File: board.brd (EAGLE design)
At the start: 100 x 80 mm, 11 parts, among them CON1 Power, SW1 PROG, SW2 RESET

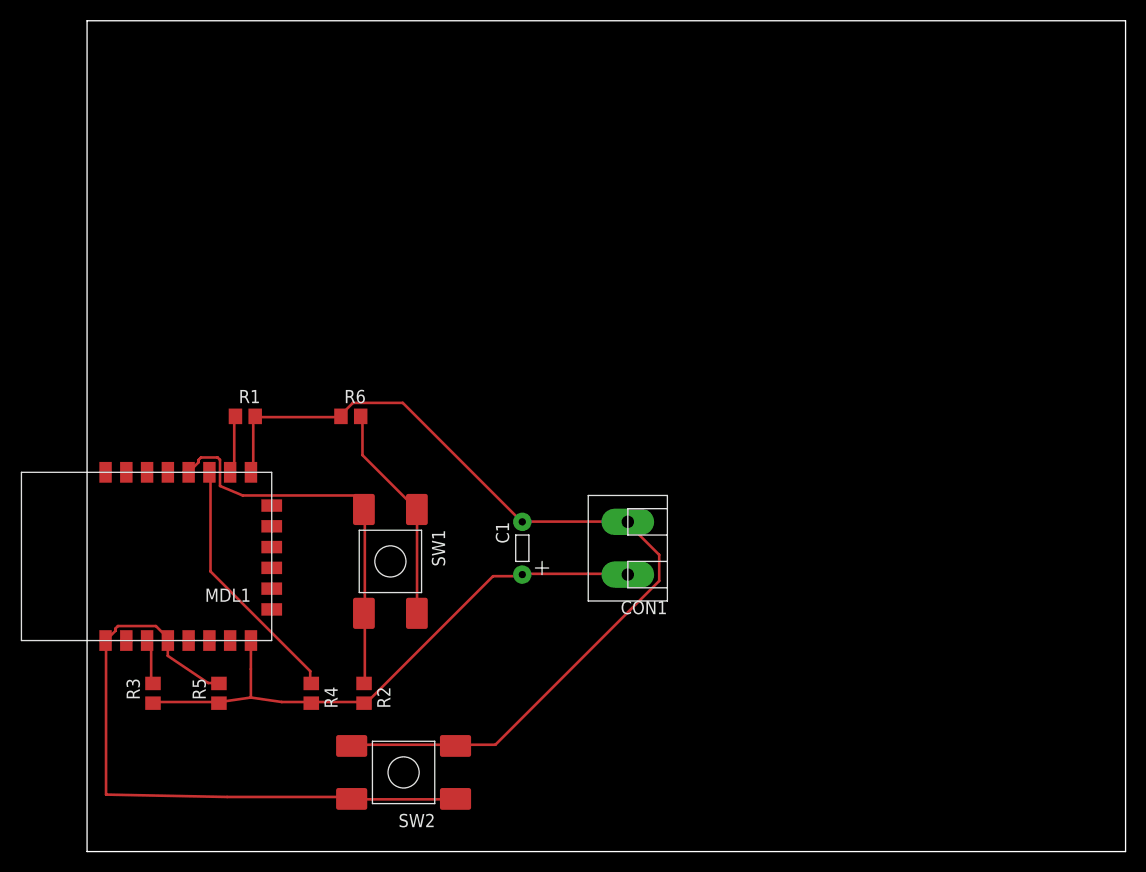
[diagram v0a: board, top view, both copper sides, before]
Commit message: Modifications last MHV meeting.
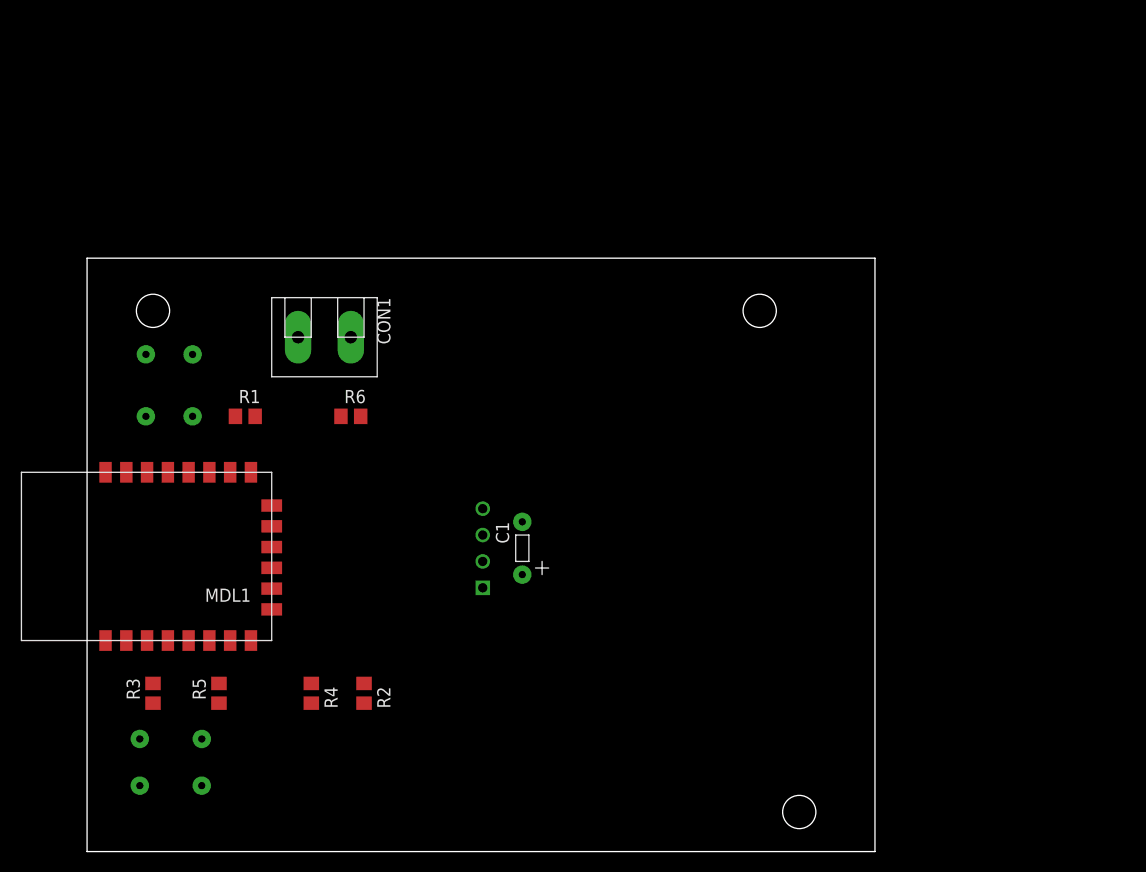
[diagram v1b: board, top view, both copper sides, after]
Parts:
- added LCD1: W128x64, my_lib:OLED_SMALL_I2C
- SW1, SW2: device steves:SWITCH-SPST-TACTILE-SMD -> steves:SWITCH-SPST-MOMENTARY
- moved CON1 36.4 mm to (20.3, 49.5), turned to 270 degrees
- moved SW2 25.4 mm to (5.08, 6.35), flipped to the bottom
- moved SW1 23.6 mm to (10.2, 41.9), flipped to the bottom, turned to 0 degrees
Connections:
- removed net N$2: MDL1.11, R4.1
- removed net N$6: MDL1.12, R2.1, SW1.P$3, SW1.P$4
- new net SCL: LCD1.SCL, MDL1.11, R4.1
- new net SDA: LCD1.SDA, MDL1.12, R2.1, SW1.P$3, SW1.P$4
- net GND: now also LCD1.GND
- net VCC: now also LCD1.VCC
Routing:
- net GND: track 90.2 -> 0.00 mm
- net N$5: track 63.6 -> 0.00 mm
- net VCC: track 56.9 -> 0.29 mm
- net N$6: track 38.7 -> 0.00 mm
- net N$2: track 24.4 -> 0.00 mm
- net N$7: track 21.3 -> 0.00 mm
- net N$1: track 5.67 -> 0.00 mm
- net N$3: track 4.42 -> 0.00 mm
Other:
- board size 100 x 80 mm -> 75.9 x 57.1 mm
